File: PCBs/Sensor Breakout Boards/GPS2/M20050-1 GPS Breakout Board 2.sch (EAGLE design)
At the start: 7 parts, among them J1 2X6 FEMALE

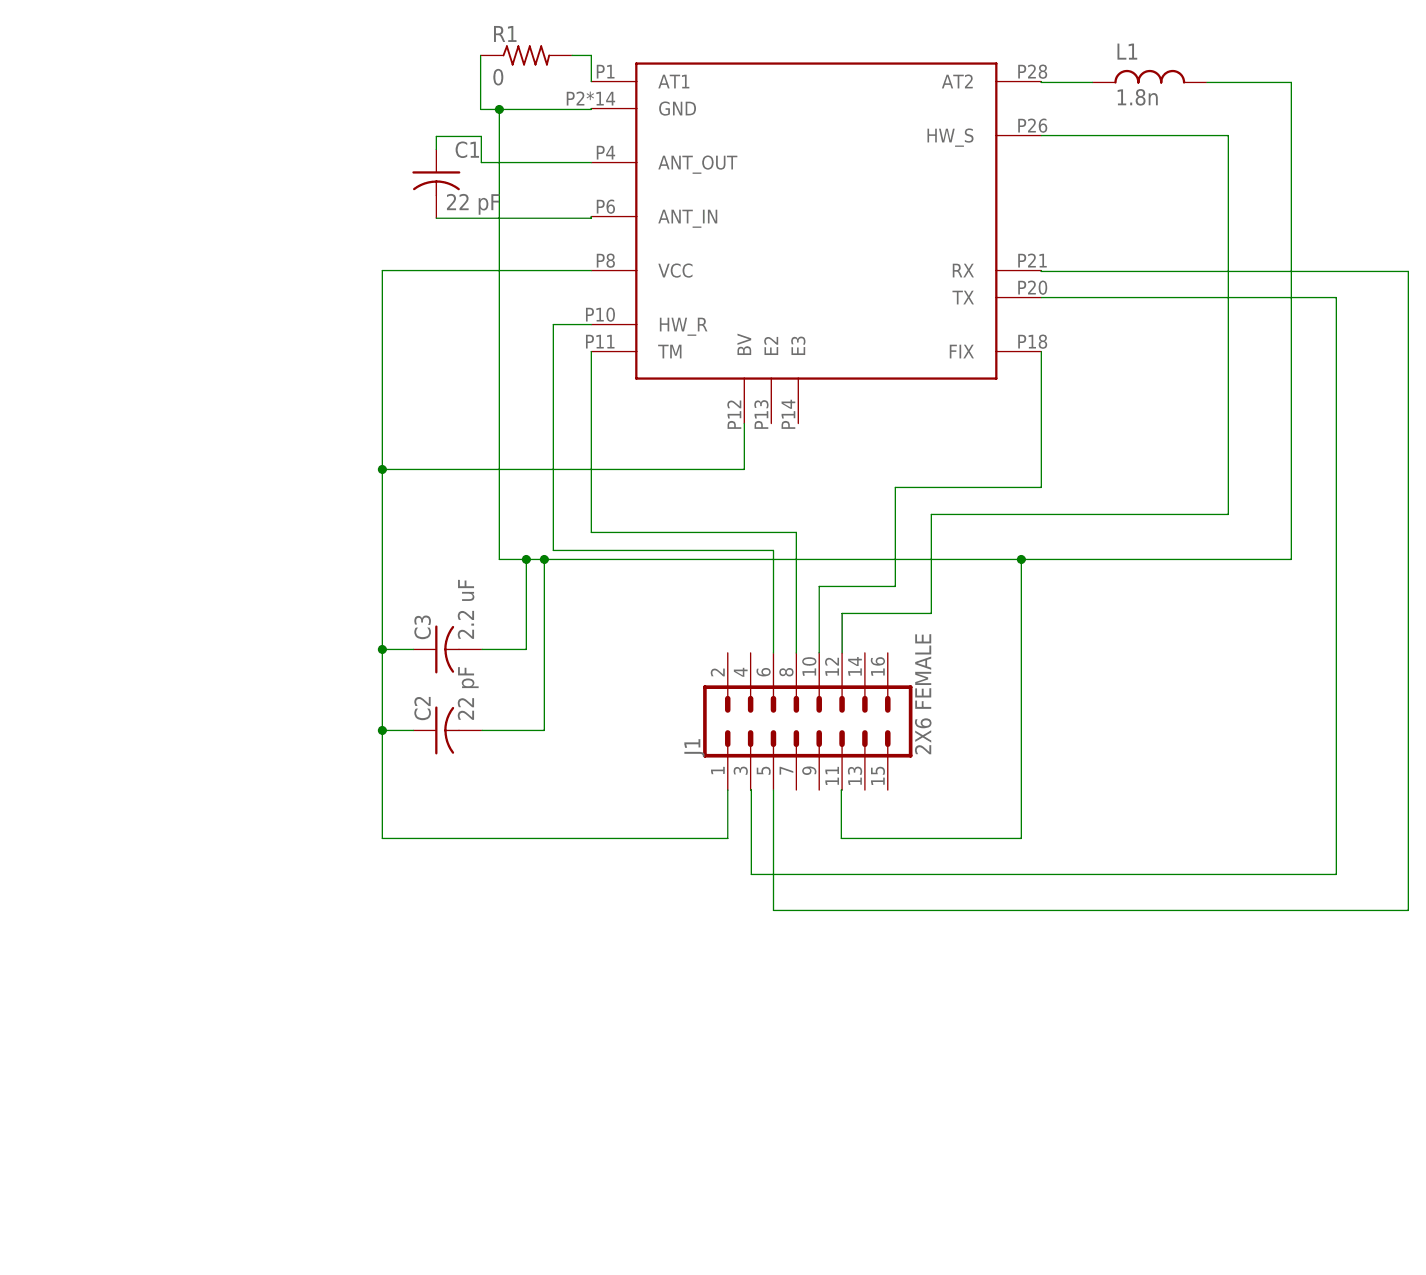
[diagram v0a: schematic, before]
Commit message: GPS2 schematic
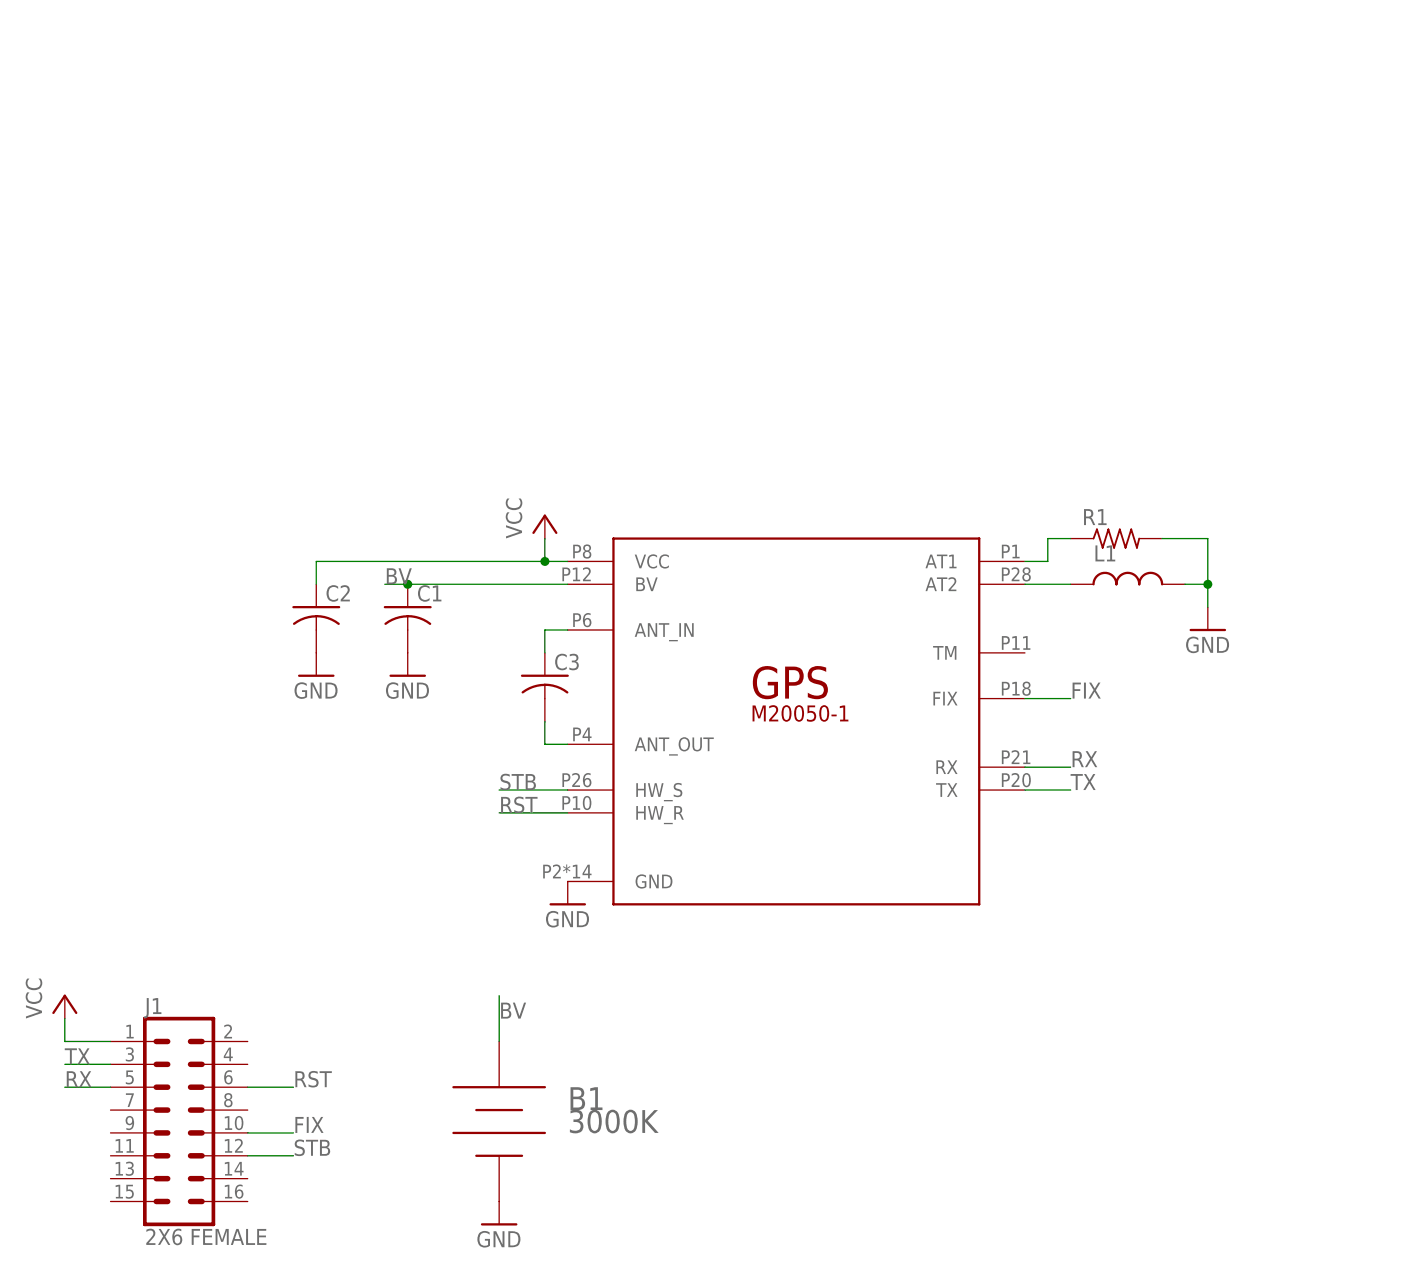
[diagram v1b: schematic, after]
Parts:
- added B1: 3000K, b_keystone_3000k_sm_battery:3000K
- A1: device RTR:GPS_M20050-1 -> M20050-1 GPS:GPS_M20050-1
- C1, C2: value 22 pF -> (none); device RTR:C-ALL_PACKAGESC1206 -> RTR Main Library:C-ALL_PACKAGESC1206
- C3: value 2.2 uF -> (none); device RTR:C-ALL_PACKAGESC1206 -> RTR Main Library:C-ALL_PACKAGESC1206
- J1: device RTR:SENSOR_BREAKOUTPTH_FEMALE -> RTR Main Library:SENSOR_BREAKOUTPTH_FEMALE
- L1: value 1.8n -> (none); device RTR:L_1206 -> RTR Main Library:L_SMD
- R1: value 0 -> (none); device RTR:R-ALL_PACKAGESM1206 -> RTR Main Library:R-ALL_PACKAGESR1206
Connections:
- net N$10 renamed RST
- net N$2 renamed TX
- net N$4 renamed RX
- net N$7 renamed STB
- net N$8 renamed FIX
- removed net N$11: A1.AT1, R1.2
- removed net N$5: A1.ANT_OUT, C1.1
- removed net N$6: A1.ANT_IN, C1.2
- removed net N$9: A1.TM, J1.8
- new net BV: A1.BV, B1.+, C1.1
- new net N$2: A1.ANT_OUT, C3.2
- new net N$3: A1.AT1, R1.1
- new net VCC: A1.VCC, C2.1, J1.1
- net GND: now also B1.-, C1.2, R1.2; no longer C3.2, J1.11, R1.1
- net N$1: now also A1.ANT_IN; no longer A1.BV, A1.VCC, C2.1, J1.1
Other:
- moved on the sheet: C1, C2, C3, J1, L1, R1

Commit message: finish gpsv2
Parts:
- C1, C3: value (none) -> 22p
- C2: value (none) -> 2.2u
- L1: value (none) -> 1.8n
- R1: value (none) -> 0R
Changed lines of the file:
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@@
 <?xml version="1.0" encoding="utf-8"?>
 <!DOCTYPE eagle SYSTEM "eagle.dtd">
-<eagle version="9.5.0">
+<eagle version="9.6.2">
 <drawing>
 <settings>
@@
 <part name="GND1" library="RTR Main Library" deviceset="GND" device=""/>
 <part name="GND2" library="RTR Main Library" deviceset="GND" device=""/>
-<part name="C1" library="RTR Main Library" deviceset="C-ALL_PACKAGES" device="C1206"/>
-<part name="C2" library="RTR Main Library" deviceset="C-ALL_PACKAGES" device="C1206"/>
-<part name="C3" library="RTR Main Library" deviceset="C-ALL_PACKAGES" device="C1206"/>
+<part name="C1" library="RTR Main Library" deviceset="C-ALL_PACKAGES" device="C1206" value="22p"/>
+<part name="C2" library="RTR Main Library" deviceset="C-ALL_PACKAGES" device="C1206" value="2.2u"/>
+<part name="C3" library="RTR Main Library" deviceset="C-ALL_PACKAGES" device="C1206" value="22p"/>
 <part name="GND3" library="RTR Main Library" deviceset="GND" device=""/>
 <part name="P+1" library="RTR Main Library" deviceset="VCC" device=""/>
 <part name="P+2" library="RTR Main Library" deviceset="VCC" device=""/>
-<part name="R1" library="RTR Main Library" deviceset="R-ALL_PACKAGES" device="R1206"/>
-<part name="L1" library="RTR Main Library" deviceset="L_SMD" device=""/>
+<part name="R1" library="RTR Main Library" deviceset="R-ALL_PACKAGES" device="R1206" value="0R"/>
+<part name="L1" library="RTR Main Library" deviceset="L_SMD" device="" value="1.8n"/>
 <part name="GND4" library="RTR Main Library" deviceset="GND" device=""/>
 <part name="GND5" library="RTR Main Library" deviceset="GND" device=""/>

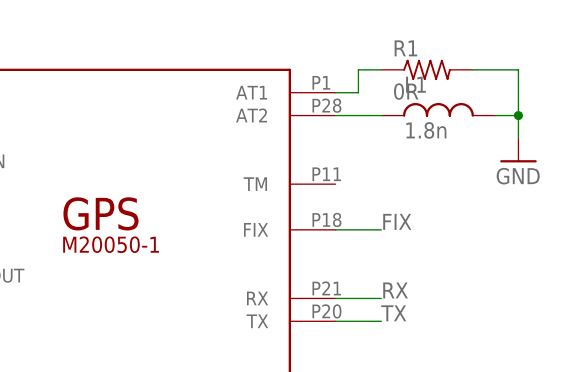
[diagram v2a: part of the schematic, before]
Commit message: update gps to work with smaller inductor
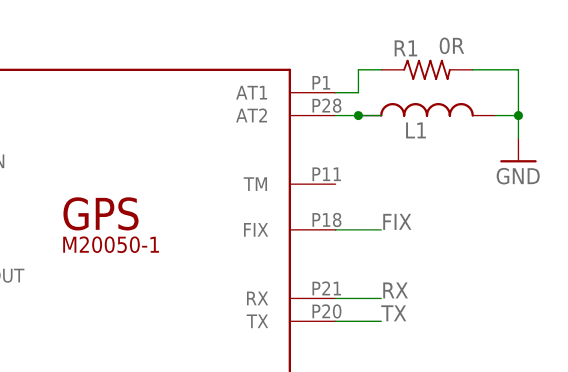
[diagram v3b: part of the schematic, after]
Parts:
- L1: device RTR Main Library:L_SMD -> AIMC-0805-1N8S-T:AIMC-0805-1N8S-T
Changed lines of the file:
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@@
 <part name="P+2" library="RTR Main Library" deviceset="VCC" device=""/>
 <part name="R1" library="RTR Main Library" deviceset="R-ALL_PACKAGES" device="R1206" value="0R"/>
-<part name="L1" library="RTR Main Library" deviceset="L_SMD" device="" value="1.8n"/>
 <part name="GND4" library="RTR Main Library" deviceset="GND" device=""/>
 <part name="GND5" library="RTR Main Library" deviceset="GND" device=""/>
+<part name="L1" library="AIMC-0805-1N8S-T" deviceset="AIMC-0805-1N8S-T" device="" value="1.8n"/>
 </parts>
 <sheets>
@@
 <instance part="R1" gate="G$1" x="35.56" y="20.32" smashed="yes">
 <attribute name="NAME" x="31.75" y="21.8186" size="1.778" layer="95"/>
-<attribute name="VALUE" x="31.75" y="17.018" size="1.778" layer="96"/>
-</instance>
-<instance part="L1" gate="G$1" x="35.56" y="15.24" smashed="yes">
-<attribute name="NAME" x="33.02" y="17.78" size="1.778" layer="95"/>
-<attribute name="VALUE" x="33.02" y="12.7" size="1.778" layer="96"/>
+<attribute name="VALUE" x="36.83" y="22.098" size="1.778" layer="96"/>
 </instance>
 <instance part="GND4" gate="1" x="-53.34" y="5.08" smashed="yes">
@@
 <instance part="GND5" gate="1" x="45.72" y="10.16" smashed="yes">
 <attribute name="VALUE" x="43.18" y="7.62" size="1.778" layer="96"/>
+</instance>
+<instance part="L1" gate="G$1" x="35.56" y="15.24" smashed="yes">
+<attribute name="NAME" x="33.02" y="12.7" size="1.778" layer="95"/>
 </instance>
 </instances>
@@
 <pinref part="GND5" gate="1" pin="GND"/>
 <wire x1="45.72" y1="20.32" x2="45.72" y2="15.24" width="0.1524" layer="91"/>
-<pinref part="L1" gate="G$1" pin="2"/>
 <wire x1="45.72" y1="15.24" x2="45.72" y2="12.7" width="0.1524" layer="91"/>
 <wire x1="43.18" y1="15.24" x2="45.72" y2="15.24" width="0.1524" layer="91"/>
 <junction x="45.72" y="15.24"/>
+<pinref part="L1" gate="G$1" pin="2"/>
 </segment>
 </net>
@@
 <segment>
 <pinref part="A1" gate="G$1" pin="AT2"/>
+<wire x1="25.4" y1="15.24" x2="27.94" y2="15.24" width="0.1524" layer="91"/>
 <pinref part="L1" gate="G$1" pin="1"/>
-<wire x1="25.4" y1="15.24" x2="30.48" y2="15.24" width="0.1524" layer="91"/>
+<wire x1="27.94" y1="15.24" x2="30.48" y2="15.24" width="0.1524" layer="91"/>
+<junction x="27.94" y="15.24"/>
 </segment>
 </net>
@@
 packages will not be understood (or retained) with this version.
 </note>
-<note version="8.4" severity="warning">
-Since Version 8.4, EAGLE supports properties for SPICE simulation.
-Probes in schematics and SPICE mapping objects found in parts and library devices
-will not be understood with this version. Update EAGLE to the latest version
-for full support of SPICE simulation.
-</note>
 </compatibility>

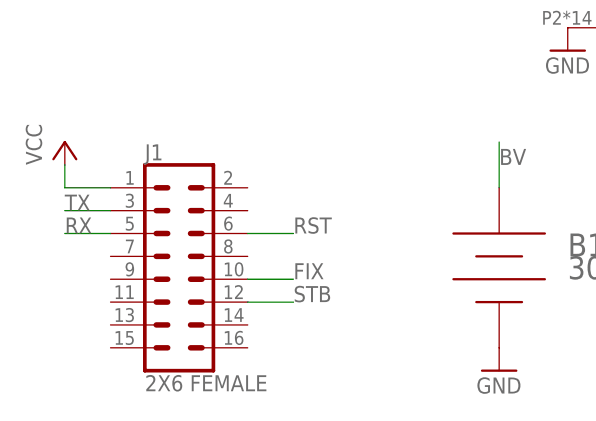
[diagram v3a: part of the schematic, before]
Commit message: fix standby and gnd gps
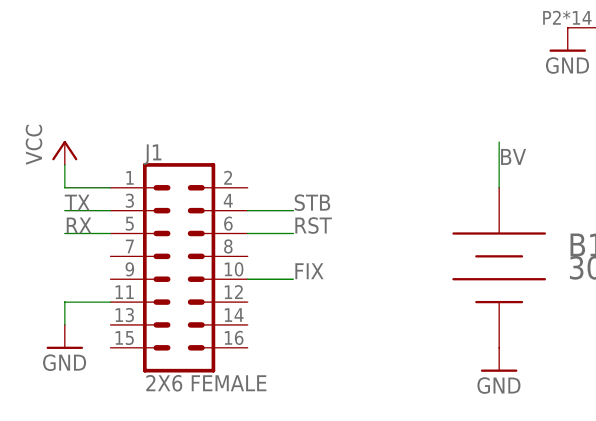
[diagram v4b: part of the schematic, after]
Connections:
- net GND: now also J1.11
- net STB: now also J1.4; no longer J1.12
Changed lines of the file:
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@@
 <part name="GND5" library="RTR Main Library" deviceset="GND" device=""/>
 <part name="L1" library="AIMC-0805-1N8S-T" deviceset="AIMC-0805-1N8S-T" device="" value="1.8n"/>
+<part name="GND6" library="RTR Main Library" deviceset="GND" device=""/>
 </parts>
 <sheets>
@@
 <attribute name="NAME" x="33.02" y="12.7" size="1.778" layer="95"/>
 </instance>
+<instance part="GND6" gate="1" x="-81.28" y="-53.34" smashed="yes">
+<attribute name="VALUE" x="-83.82" y="-55.88" size="1.778" layer="96"/>
+</instance>
 </instances>
 <busses>
@@
 <pinref part="L1" gate="G$1" pin="2"/>
 </segment>
+<segment>
+<pinref part="GND6" gate="1" pin="GND"/>
+<wire x1="-81.28" y1="-50.8" x2="-81.28" y2="-48.26" width="0.1524" layer="91"/>
+<pinref part="J1" gate="G$1" pin="11"/>
+<wire x1="-81.28" y1="-48.26" x2="-76.2" y2="-48.26" width="0.1524" layer="91"/>
+</segment>
 </net>
 <net name="N$1" class="0">
@@
 <net name="STB" class="0">
 <segment>
-<pinref part="J1" gate="G$1" pin="12"/>
-<wire x1="-60.96" y1="-48.26" x2="-55.88" y2="-48.26" width="0.1524" layer="91"/>
-<label x="-55.88" y="-48.26" size="1.778" layer="95"/>
-</segment>
-<segment>
 <pinref part="A1" gate="G$1" pin="HW_S"/>
 <wire x1="-25.4" y1="-7.62" x2="-33.02" y2="-7.62" width="0.1524" layer="91"/>
 <label x="-33.02" y="-7.62" size="1.778" layer="95"/>
 </segment>
-</net>
+<segment>
+<pinref part="J1" gate="G$1" pin="4"/>
+<wire x1="-60.96" y1="-38.1" x2="-55.88" y2="-38.1" width="0.1524" layer="91"/>
+<label x="-55.88" y="-38.1" size="1.778" layer="95"/>
+</segment>
+</net>
